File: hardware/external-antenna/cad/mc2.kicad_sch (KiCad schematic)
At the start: 21 parts, among them J1 FUSED ISOLATED 5V INPUT, J2 D24V22F3 external assembled b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, J3 DFR0627 WK2132 ready module h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, J4 ZAC93 ready module harness, J5 CC1101 ready module harness, J6 LD2450 radar harness, J7 BME680 external pod harness, J8 XIAO BOOT unpopulated service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, J9 HOST BOOT unpopulated service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, U1 ESP32-DevKitC-VIE, U2 Unexpected Maker TinyC6[D] TC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, U3 Seeed XIAO MG24 pre-soldered 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, U4 WIZ850io finished module

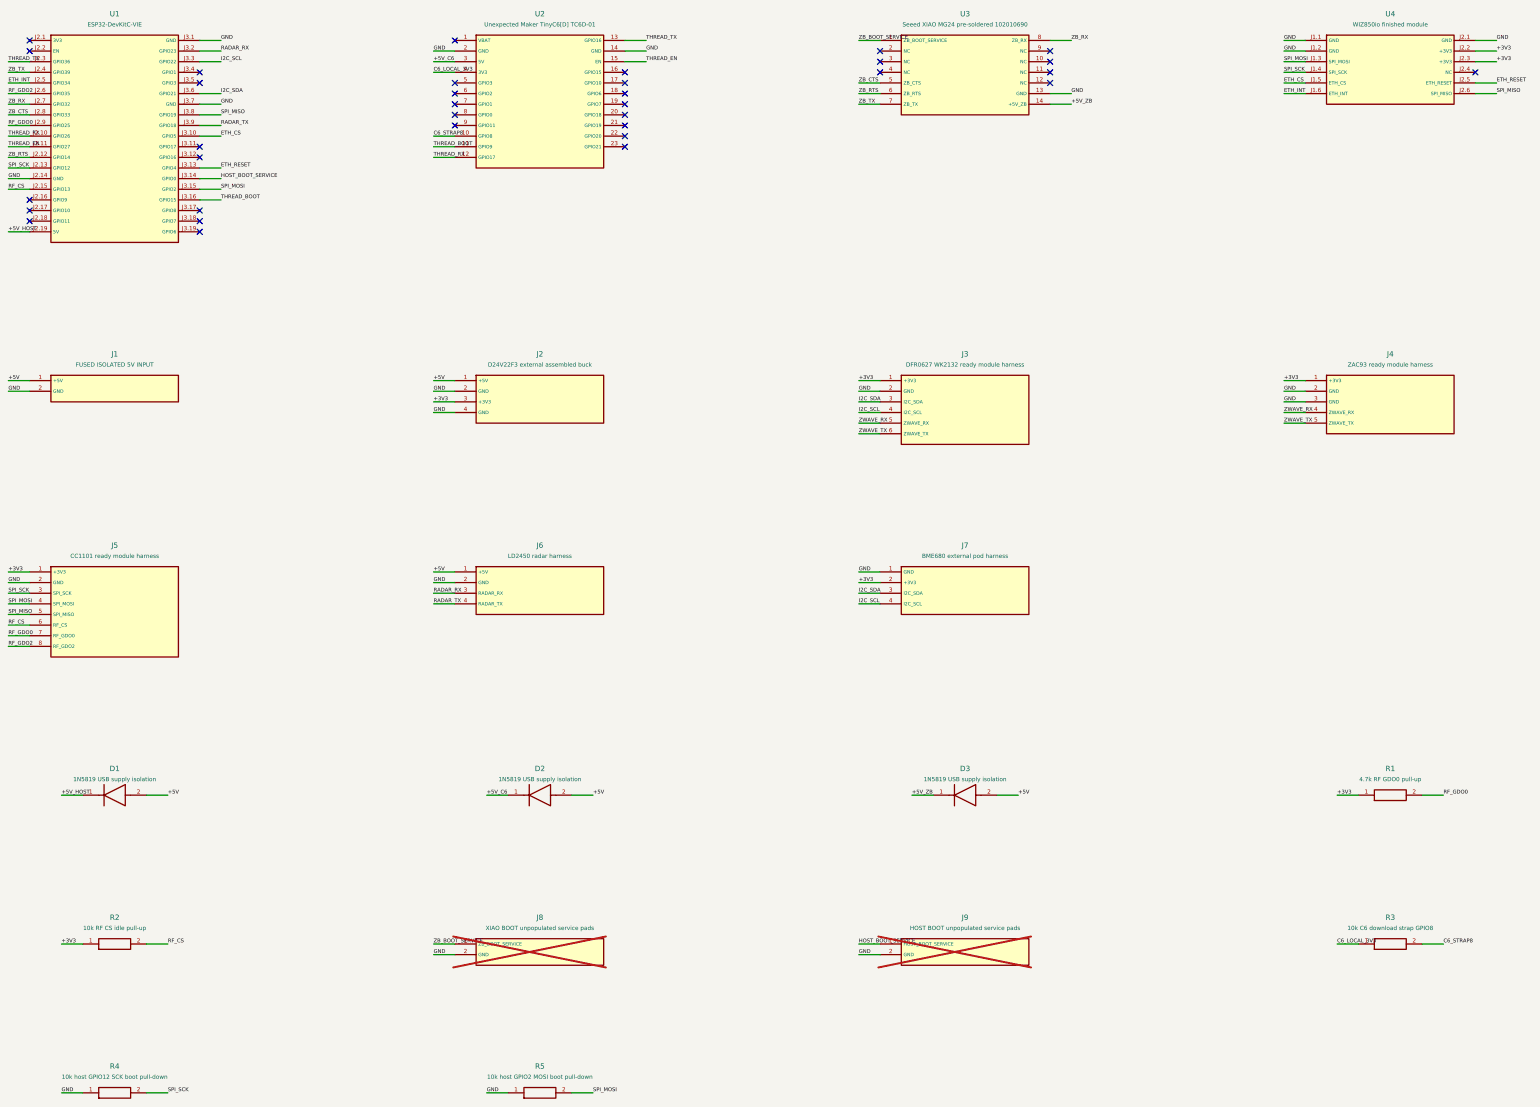
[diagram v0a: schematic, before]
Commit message: Use factory-header XIAO ESP32C6 and fix I2C/RF conflicts (#21)
MC2-D replaces the unpurchased TinyC6[D] with the US-distributed,
factory-header Seeed XIAO ESP32C6 (102010636), retaining the ordered
ESP32-DevKitC-VIE and the existing hub functions. The new carrier
includes the XIAO footprint, J10 recovery leads and an underside access
window; firmware and assembly models match its 4 MB flash and
external-antenna control.

An independent connection audit also found an I2C collision: the DFR0627
setting A1=1/A0=1 decodes 0x70–0x77, including BME680. Both maintained
MC2 and MC1 firmware profiles now use A1=1/A0=0, UART1 register/FIFO
0x50/0x51, reserving 0x50–0x57. Configuration validation rejects another
device in the bridge's entire address block. Assembly instructions,
current wiring graphics and CAD metadata carry the corrected switch
setting. This address correction changes no PCB copper or print
geometry.

The audit also found an RMT startup contention window on CC1101 GDO0. A
local, version-guarded initialization wrapper releases the configured RF
pin and sets HIGH idle before the driver connects its output; the shared
RF package uses it without an upstream fork or SDK cache changes. Other
transmitter pins retain their normal allocation path. Runtime handoff
also requires GDO0 high-impedance readback and confirmed IDLE/TX states
before the waveform; failed transitions release the line and skip
transmission, and RX restoration is verified.

The final purchase audit confirms all 28 submitted DigiKey lines and the
Mouser ESP32-DevKitC-VIE against the MC2-D interfaces. It also removes
the avoidable Schottky drop before the host AMS1117: the legacy D1 pads
now take an insulated 22 AWG wire link, labelled NO DIODE. D2/D3 remain
1N5819, so the third purchased diode is a spare. The copper topology is
unchanged. The assembled hub uses PoE/OTA only; host USB could feed the
full 5 V bus through the link. ZAC93 instructions explicitly require
soldering the harness to the ada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
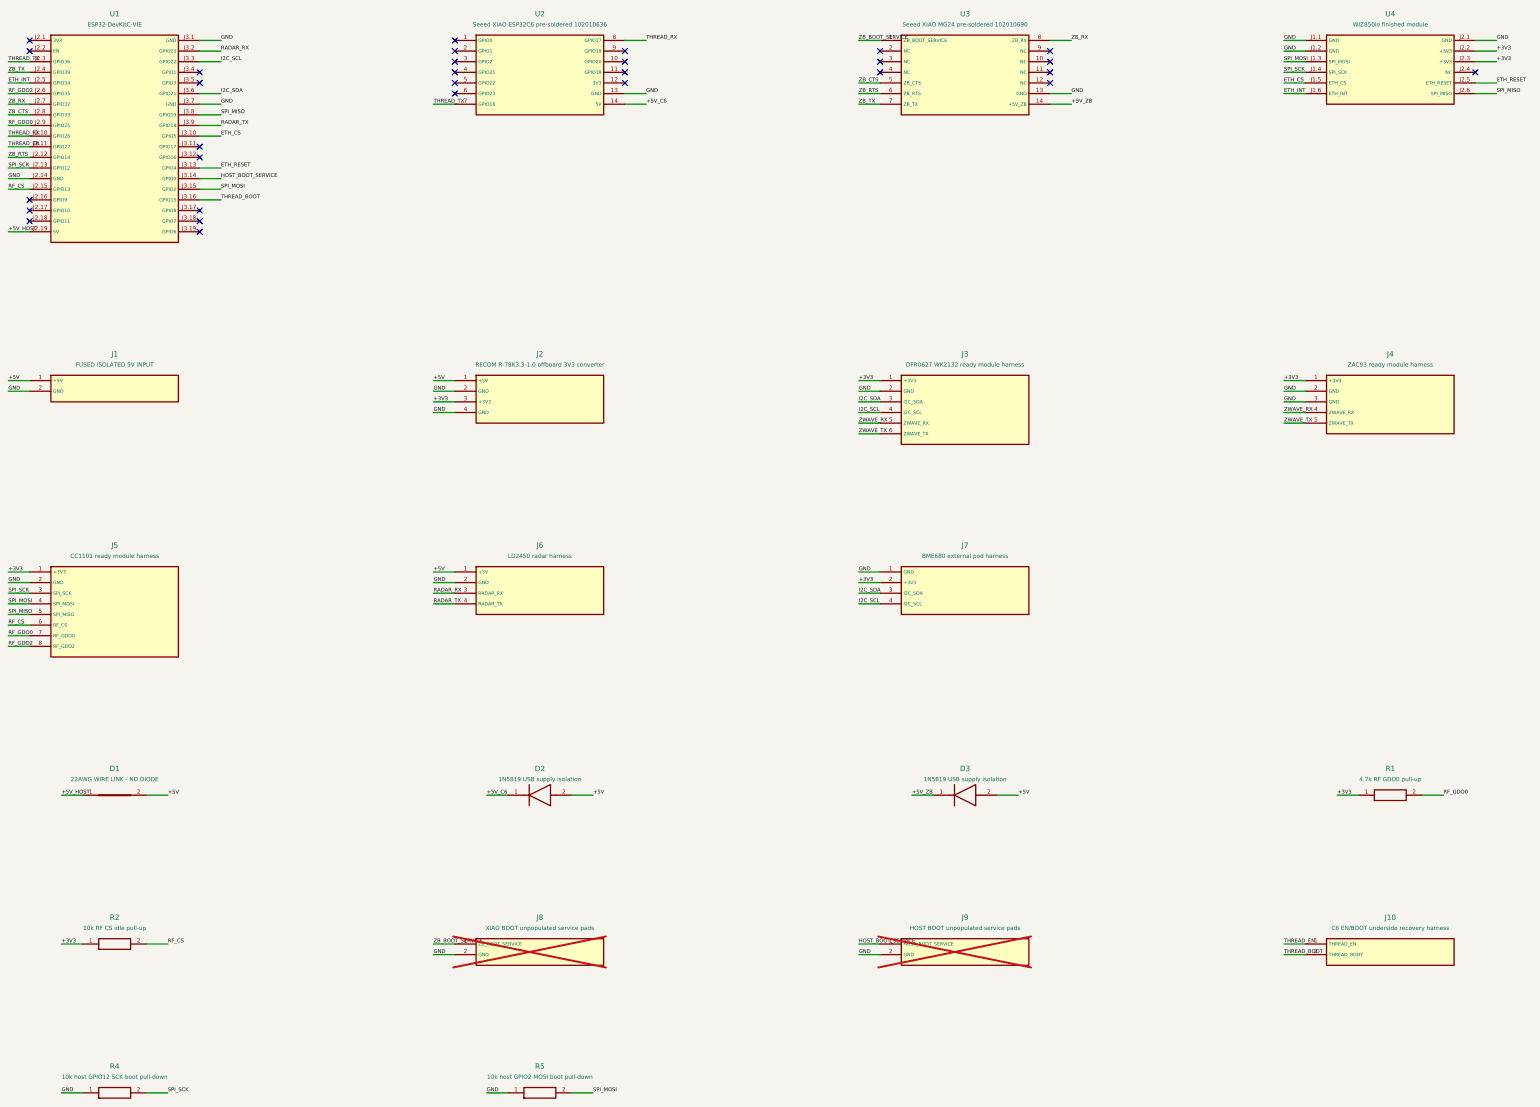
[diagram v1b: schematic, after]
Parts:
- removed R3: 10k C6 download strap GPIO8, MC2:R_Axial_DIN0207_L6.3mm_D2.5mm_P7.62mm_Horizontal, symbol MC2:Module_R3
- added J10: C6 EN/BOOT underside recovery harness, MC2:PinHeader_1x02_P2.54mm_Vertical, symbol MC2:Module_J10
- D1: value 1N5819 USB supply isolation -> 22AWG WIRE LINK - NO DIODE; footprint MC2:D_DO-41_SOD81_P7.62mm_Horizontal -> MC2:Wire_Link_P7.62mm
- J2: value D24V22F3 external assembled buck -> RECOM R-78K3.3-1.0 offboard 3V3 converter
- U2: value Unexpected Maker TinyC6[D] TC6D-01 -> Seeed XIAO ESP32C6 pre-soldered 102010636; footprint MC2:TinyC6_D -> MC2:XIAO_ESP32C6
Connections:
- net +5V_C6: now also U2.14 (5V); no longer U2.3 (5V)
- net GND: now also U2.13 (GND); no longer U2.14 (GND), U2.2 (GND)
- net THREAD_BOOT: now also J10.2 (THREAD_BOOT); no longer U2.11 (GPIO9)
- net THREAD_EN: now also J10.1 (THREAD_EN); no longer U2.15 (EN)
- net THREAD_RX: now also U2.8 (GPIO17); no longer U2.12 (GPIO17)
- net THREAD_TX: now also U2.7 (GPIO16); no longer U2.13 (GPIO16)
- net C6_LOCAL_3V3: no longer names the net of U2.4 (GPIO21)
- net C6_STRAP8: no longer names the net of U2.10 (GPIO20)
- no-connect marks 34 -> 30
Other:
- title: MC2-C ESP32 external antennas - engineering prototype -> MC2-D ESP32 external antennas - engineering prototype
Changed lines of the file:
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@@
-(kicad_sch (version 20250114) (generator "eeschema") (paper "A3") (title_block (title "MC2-C ESP32 external antennas - engineering prototype") (date "2026-10-19") (rev "MC2-C") (comment 1 "Direct-solder THT male pins; all parts front; no carrier SMT") (comment 2 "External isolated fused 5V; separate peripheral 3V3; module 3V3 outputs never joined"))
+(kicad_sch (version 20250114) (generator "eeschema") (paper "A3") (title_block (title "MC2-D ESP32 external antennas - engineering prototype") (date "2026-10-20") (rev "MC2-D") (comment 1 "Direct-solder THT male pins; all parts front; no carrier SMT") (comment 2 "External isolated fused 5V; separate peripheral 3V3; module 3V3 outputs never joined"))
 (wire (pts (xy 25.4 35.56) (xy 20.32 35.56)) (stroke (width 0) (type default)))
 (wire (pts (xy 25.4 38.1) (xy 20.32 38.1)) (stroke (width 0) (type default)))
@@
 (wire (pts (xy 66.04 66.04) (xy 71.12 66.04)) (stroke (width 0) (type default)))
 (wire (pts (xy 66.04 68.58) (xy 71.12 68.58)) (stroke (width 0) (type default)))
-(wire (pts (xy 127.0 33.02) (xy 121.92 33.02)) (stroke (width 0) (type default)))
-(wire (pts (xy 127.0 35.56) (xy 121.92 35.56)) (stroke (width 0) (type default)))
-(wire (pts (xy 127.0 38.1) (xy 121.92 38.1)) (stroke (width 0) (type default)))
-(wire (pts (xy 127.0 53.34) (xy 121.92 53.34)) (stroke (width 0) (type default)))
-(wire (pts (xy 127.0 55.88) (xy 121.92 55.88)) (stroke (width 0) (type default)))
-(wire (pts (xy 127.0 58.42) (xy 121.92 58.42)) (stroke (width 0) (type default)))
+(wire (pts (xy 127.0 45.72) (xy 121.92 45.72)) (stroke (width 0) (type default)))
 (wire (pts (xy 167.64 30.48) (xy 172.72 30.48)) (stroke (width 0) (type default)))
-(wire (pts (xy 167.64 33.02) (xy 172.72 33.02)) (stroke (width 0) (type default)))
-(wire (pts (xy 167.64 35.56) (xy 172.72 35.56)) (stroke (width 0) (type default)))
+(wire (pts (xy 167.64 43.18) (xy 172.72 43.18)) (stroke (width 0) (type default)))
+(wire (pts (xy 167.64 45.72) (xy 172.72 45.72)) (stroke (width 0) (type default)))
 (wire (pts (xy 228.6 30.48) (xy 223.52 30.48)) (stroke (width 0) (type default)))
 (wire (pts (xy 228.6 40.64) (xy 223.52 40.64)) (stroke (width 0) (type default)))
@@
 (wire (pts (xy 228.6 246.38) (xy 223.52 246.38)) (stroke (width 0) (type default)))
 (wire (pts (xy 228.6 248.92) (xy 223.52 248.92)) (stroke (width 0) (type default)))
-(wire (pts (xy 342.9 246.38) (xy 337.82 246.38)) (stroke (width 0) (type default)))
-(wire (pts (xy 358.14 246.38) (xy 363.22 246.38)) (stroke (width 0) (type default)))
+(wire (pts (xy 330.2 246.38) (xy 325.12 246.38)) (stroke (width 0) (type default)))
+(wire (pts (xy 330.2 248.92) (xy 325.12 248.92)) (stroke (width 0) (type default)))
 (wire (pts (xy 38.1 281.94) (xy 33.02 281.94)) (stroke (width 0) (type default)))
 (wire (pts (xy 53.34 281.94) (xy 58.42 281.94)) (stroke (width 0) (type default)))
@@
 (label "SPI_MOSI" (at 71.12 66.04 0) (effects (font (size 0.9 0.9)) (justify left bottom)))
 (label "THREAD_BOOT" (at 71.12 68.58 0) (effects (font (size 0.9 0.9)) (justify left bottom)))
-(label "GND" (at 121.92 33.02 180) (effects (font (size 0.9 0.9)) (justify left bottom)))
-(label "+5V_C6" (at 121.92 35.56 180) (effects (font (size 0.9 0.9)) (justify left bottom)))
-(label "C6_LOCAL_3V3" (at 121.92 38.1 180) (effects (font (size 0.9 0.9)) (justify left bottom)))
-(label "C6_STRAP8" (at 121.92 53.34 180) (effects (font (size 0.9 0.9)) (justify left bottom)))
-(label "THREAD_BOOT" (at 121.92 55.88 180) (effects (font (size 0.9 0.9)) (justify left bottom)))
-(label "THREAD_RX" (at 121.92 58.42 180) (effects (font (size 0.9 0.9)) (justify left bottom)))
-(label "THREAD_TX" (at 172.72 30.48 0) (effects (font (size 0.9 0.9)) (justify left bottom)))
-(label "GND" (at 172.72 33.02 0) (effects (font (size 0.9 0.9)) (justify left bottom)))
-(label "THREAD_EN" (at 172.72 35.56 0) (effects (font (size 0.9 0.9)) (justify left bottom)))
+(label "THREAD_TX" (at 121.92 45.72 180) (effects (font (size 0.9 0.9)) (justify left bottom)))
+(label "THREAD_RX" (at 172.72 30.48 0) (effects (font (size 0.9 0.9)) (justify left bottom)))
+(label "GND" (at 172.72 43.18 0) (effects (font (size 0.9 0.9)) (justify left bottom)))
+(label "+5V_C6" (at 172.72 45.72 0) (effects (font (size 0.9 0.9)) (justify left bottom)))
 (label "ZB_BOOT_SERVICE" (at 223.52 30.48 180) (effects (font (size 0.9 0.9)) (justify left bottom)))
 (label "ZB_CTS" (at 223.52 40.64 180) (effects (font (size 0.9 0.9)) (justify left bottom)))
@@
 (label "HOST_BOOT_SERVICE" (at 223.52 246.38 180) (effects (font (size 0.9 0.9)) (justify left bottom)))
 (label "GND" (at 223.52 248.92 180) (effects (font (size 0.9 0.9)) (justify left bottom)))
-(label "C6_LOCAL_3V3" (at 337.82 246.38 180) (effects (font (size 0.9 0.9)) (justify left bottom)))
-(label "C6_STRAP8" (at 363.22 246.38 0) (effects (font (size 0.9 0.9)) (justify left bottom)))
+(label "THREAD_EN" (at 325.12 246.38 180) (effects (font (size 0.9 0.9)) (justify left bottom)))
+(label "THREAD_BOOT" (at 325.12 248.92 180) (effects (font (size 0.9 0.9)) (justify left bottom)))
 (label "GND" (at 33.02 281.94 180) (effects (font (size 0.9 0.9)) (justify left bottom)))
 (label "SPI_SCK" (at 58.42 281.94 0) (effects (font (size 0.9 0.9)) (justify left bottom)))
@@
 (no_connect (at 66.04 76.2))
 (no_connect (at 127.0 30.48))
+(no_connect (at 127.0 33.02))
+(no_connect (at 127.0 35.56))
+(no_connect (at 127.0 38.1))
 (no_connect (at 127.0 40.64))
 (no_connect (at 127.0 43.18))
-(no_connect (at 127.0 45.72))
-(no_connect (at 127.0 48.26))
-(no_connect (at 127.0 50.8))
+(no_connect (at 167.64 33.02))
+(no_connect (at 167.64 35.56))
 (no_connect (at 167.64 38.1))
 (no_connect (at 167.64 40.64))
-(no_connect (at 167.64 43.18))
-(no_connect (at 167.64 45.72))
-(no_connect (at 167.64 48.26))
-(no_connect (at 167.64 50.8))
-(no_connect (at 167.64 53.34))
-(no_connect (at 167.64 55.88))
 (no_connect (at 228.6 33.02))
 (no_connect (at 228.6 35.56))
@@
 (symbol (lib_id "MC2:Module_U2") (at 147.3200 30.4800 0) (unit 1) (in_bom yes) (on_board yes) (dnp no)
 (property "Reference" "U2" (at 147.32 24.130000000000003 0) (effects (font (size 1.27 1.27))))
-(property "Value" "Unexpected Maker TinyC6[D] TC6D-01" (at 147.32 26.67 0) (effects (font (size 1 1))))
-(property "Footprint" "MC2:TinyC6_D" (at 147.32 30.48 0) (effects (font (size 1 1)) hide))
+(property "Value" "Seeed XIAO ESP32C6 pre-soldered 102010636" (at 147.32 26.67 0) (effects (font (size 1 1))))
+(property "Footprint" "MC2:XIAO_ESP32C6" (at 147.32 30.48 0) (effects (font (size 1 1)) hide))
 (pin "1")
 (pin "2")
@@
 (pin "13")
 (pin "14")
-(pin "15")
-(pin "16")
-(pin "17")
-(pin "18")
-(pin "19")
-(pin "20")
-(pin "21")
-(pin "22")
-(pin "23")
 (instances (project "mc2" (path "/24581fcf-1632-59ed-8931-7790c5d2febc" (reference "U2") (unit 1)))))
 (symbol (lib_id "MC2:Module_U3") (at 248.9200 30.4800 0) (unit 1) (in_bom yes) (on_board yes) (dnp no)
@@
 (symbol (lib_id "MC2:Module_J2") (at 147.3200 111.7600 0) (unit 1) (in_bom yes) (on_board yes) (dnp no)
 (property "Reference" "J2" (at 147.32 105.41000000000001 0) (effects (font (size 1.27 1.27))))
-(property "Value" "D24V22F3 external assembled buck" (at 147.32 107.95 0) (effects (font (size 1 1))))
+(property "Value" "RECOM R-78K3.3-1.0 offboard 3V3 converter" (at 147.32 107.95 0) (effects (font (size 1 1))))
 (property "Footprint" "MC2:PinHeader_1x04_P2.54mm_Vertical" (at 147.32 111.76 0) (effects (font (size 1 1)) hide))
 (pin "1")
@@
 (symbol (lib_id "MC2:Module_D1") (at 45.7200 210.8200 0) (unit 1) (in_bom yes) (on_board yes) (dnp no)
 (property "Reference" "D1" (at 45.72 204.47 0) (effects (font (size 1.27 1.27))))
-(property "Value" "1N5819 USB supply isolation" (at 45.72 207.01 0) (effects (font (size 1 1))))
-(property "Footprint" "MC2:D_DO-41_SOD81_P7.62mm_Horizontal" (at 45.72 210.82 0) (effects (font (size 1 1)) hide))
+(property "Value" "22AWG WIRE LINK - NO DIODE" (at 45.72 207.01 0) (effects (font (size 1 1))))
+(property "Footprint" "MC2:Wire_Link_P7.62mm" (at 45.72 210.82 0) (effects (font (size 1 1)) hide))
 (pin "1")
 (pin "2")
@@
 (pin "2")
 (instances (project "mc2" (path "/24581fcf-1632-59ed-8931-7790c5d2febc" (reference "J9") (unit 1)))))
-(symbol (lib_id "MC2:Module_R3") (at 350.5200 246.3800 0) (unit 1) (in_bom yes) (on_board yes) (dnp no)
-(property "Reference" "R3" (at 350.52 240.03 0) (effects (font (size 1.27 1.27))))
-(property "Value" "10k C6 download strap GPIO8" (at 350.52 242.57 0) (effects (font (size 1 1))))
-(property "Footprint" "MC2:R_Axial_DIN0207_L6.3mm_D2.5mm_P7.62mm_Horizontal" (at 350.52 246.38 0) (effects (font (size 1 1)) hide))
-(pin "1")
-(pin "2")
-(instances (project "mc2" (path "/24581fcf-1632-59ed-8931-7790c5d2febc" (reference "R3") (unit 1)))))
+(symbol (lib_id "MC2:Module_J10") (at 350.5200 246.3800 0) (unit 1) (in_bom yes) (on_board yes) (dnp no)
+(property "Reference" "J10" (at 350.52 240.03 0) (effects (font (size 1.27 1.27))))
+(property "Value" "C6 EN/BOOT underside recovery harness" (at 350.52 242.57 0) (effects (font (size 1 1))))
+(property "Footprint" "MC2:PinHeader_1x02_P2.54mm_Vertical" (at 350.52 246.38 0) (effects (font (size 1 1)) hide))
+(pin "1")
+(pin "2")
+(instances (project "mc2" (path "/24581fcf-1632-59ed-8931-7790c5d2febc" (reference "J10") (unit 1)))))
 (symbol (lib_id "MC2:Module_R4") (at 45.7200 281.9400 0) (unit 1) (in_bom yes) (on_board yes) (dnp no)
 (property "Reference" "R4" (at 45.72 275.59 0) (effects (font (size 1.27 1.27))))
